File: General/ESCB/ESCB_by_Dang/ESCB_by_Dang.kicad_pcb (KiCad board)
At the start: 2 copper layers, 54.6 x 20.3 mm, 3 parts, among them J1 Power_Signal, J2 Motor

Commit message: Update
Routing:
- net GND: track 39.1 -> 41.2 mm
- net VCC: track 9.18 -> 10.7 mm
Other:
- board size 54.6 x 20.3 mm -> 52.6 x 20.3 mm
- net class Power: trace_width 0.5 -> 1
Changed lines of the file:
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@@
     (thickness 1.6)
     (drawings 7)
-    (tracks 22)
+    (tracks 24)
     (zones 0)
     (modules 3)
@@
   (net_class Power ""
     (clearance 0.2)
-    (trace_width 0.5)
+    (trace_width 1)
     (via_dia 0.8)
     (via_drill 0.4)
@@
     )
     (fp_text value Power_Signal (at 0 4.39 270) (layer F.Fab)
+      (effects (font (size 1 1) (thickness 0.15)))
+    )
+    (fp_circle (center -2 3.81) (end -1.9 3.81) (layer F.SilkS) (width 0.2))
+    (fp_circle (center -2 3.81) (end -1.9 3.81) (layer F.Fab) (width 0.2))
+    (fp_line (start -5.525 -3.1) (end 5.525 -3.1) (layer F.Fab) (width 0.1))
+    (fp_line (start 5.525 -3.1) (end 5.525 -2.4) (layer F.Fab) (width 0.1))
+    (fp_line (start 5.525 -2.4) (end 4.825 -2.4) (layer F.Fab) (width 0.1))
+    (fp_line (start 4.825 -2.4) (end 4.825 3.1) (layer F.Fab) (width 0.1))
+    (fp_line (start 4.825 3.1) (end -4.825 3.1) (layer F.Fab) (width 0.1))
+    (fp_line (start -4.825 3.1) (end -4.825 -2.4) (layer F.Fab) (width 0.1))
+    (fp_line (start -4.825 -2.4) (end -5.525 -2.4) (layer F.Fab) (width 0.1))
+    (fp_line (start -5.525 -2.4) (end -5.525 -3.1) (layer F.Fab) (width 0.1))
+    (fp_line (start -6.2 -3.35) (end 6.2 -3.35) (layer F.CrtYd) (width 0.05))
+    (fp_line (start 6.2 -3.35) (end 6.2 3.35) (layer F.CrtYd) (width 0.05))
+    (fp_line (start 6.2 3.35) (end -6.2 3.35) (layer F.CrtYd) (width 0.05))
+    (fp_line (start -6.2 3.35) (end -6.2 -3.35) (layer F.CrtYd) (width 0.05))
+    (fp_line (start -3.1 -3.1) (end 3.1 -3.1) (layer F.SilkS) (width 0.2))
+    (fp_line (start 4.825 3.1) (end -4.825 3.1) (layer F.SilkS) (width 0.2))
+    (fp_poly (pts (xy 3.5 -2.63) (xy 5.95 -2.63) (xy 5.95 -0.35) (xy 3.5 -0.35)) (layer F.Paste) (width 0.01))
+    (fp_poly (pts (xy 3.5 0.35) (xy 5.95 0.35) (xy 5.95 2.63) (xy 3.5 2.63)) (layer F.Paste) (width 0.01))
+    (fp_poly (pts (xy -5.95 -0.15) (xy -3.5 -0.15) (xy -3.5 2.13) (xy -5.95 2.13)) (layer F.Paste) (width 0.01))
+    (fp_poly (pts (xy -5.95 -3.13) (xy -3.5 -3.13) (xy -3.5 -0.85) (xy -5.95 -0.85)) (layer F.Paste) (width 0.01))
+    (pad 1 smd rect (at -2 0 270) (size 1.3 3.5) (layers F.Cu F.Paste F.Mask)
+      (net 1 GND))
+    (pad 2 smd rect (at 0 0 270) (size 1.3 3.5) (layers F.Cu F.Paste F.Mask)
+      (net 2 VCC))
+    (pad "" thru_hole circle (at -4 -1.5 270) (size 1.308 1.308) (drill 0.8) (layers *.Cu *.Mask))
+    (pad "" thru_hole circle (at -4 0.5 270) (size 1.308 1.308) (drill 0.8) (layers *.Cu *.Mask))
+    (pad "" thru_hole circle (at 4 -1 270) (size 1.308 1.308) (drill 0.8) (layers *.Cu *.Mask))
+    (pad "" thru_hole circle (at 4 1 270) (size 1.308 1.308) (drill 0.8) (layers *.Cu *.Mask))
+    (pad 3 smd rect (at 2 0 270) (size 1.3 3.5) (layers F.Cu F.Paste F.Mask)
+      (net 3 "Net-(J1-Pad3)"))
+    (model :extraparts3d:UMPS-03-03.5-T-VT-SM-WT.stp
+      (at (xyz 0 0 0))
+      (scale (xyz 1 1 1))
+      (rotate (xyz -90 0 0))
+    )
+  )
+  (module extraparts:Samtec_mPOWER_UMPS_3pin (layer F.Cu)
+    (at 164.9 93.98 90)
+    (fp_text reference J2 (at 7.62 -2.34) (layer F.SilkS)
+      (effects (font (size 1 1) (thickness 0.15)))
+    )
+    (fp_text value Motor (at 0 5.28 90) (layer F.Fab)
       (effects (font (size 1 1) (thickness 0.15)))
     )
@@
     (fp_circle (center -2 3.81) (end -1.9 3.81) (layer F.Fab) (width 0.2))
     (fp_circle (center -2 3.81) (end -1.9 3.81) (layer F.SilkS) (width 0.2))
-    (pad 1 smd rect (at -2 0 270) (size 1.3 3.5) (layers F.Cu F.Paste F.Mask)
-      (net 1 GND))
-    (pad 2 smd rect (at 0 0 270) (size 1.3 3.5) (layers F.Cu F.Paste F.Mask)
-      (net 2 VCC))
-    (pad "" thru_hole circle (at -4 -1.5 270) (size 1.308 1.308) (drill 0.8) (layers *.Cu *.Mask))
-    (pad "" thru_hole circle (at -4 0.5 270) (size 1.308 1.308) (drill 0.8) (layers *.Cu *.Mask))
-    (pad "" thru_hole circle (at 4 -1 270) (size 1.308 1.308) (drill 0.8) (layers *.Cu *.Mask))
-    (pad "" thru_hole circle (at 4 1 270) (size 1.308 1.308) (drill 0.8) (layers *.Cu *.Mask))
-    (pad 3 smd rect (at 2 0 270) (size 1.3 3.5) (layers F.Cu F.Paste F.Mask)
-      (net 3 "Net-(J1-Pad3)"))
-    (model :extraparts3d:UMPS-03-03.5-T-VT-SM-WT.stp
-      (at (xyz 0 0 0))
-      (scale (xyz 1 1 1))
-      (rotate (xyz -90 0 0))
-    )
-  )
-  (module extraparts:Samtec_mPOWER_UMPS_3pin (layer F.Cu)
-    (at 164.9 93.98 90)
-    (fp_text reference J2 (at -3.81 5.28 270) (layer F.SilkS)
-      (effects (font (size 1 1) (thickness 0.15)))
-    )
-    (fp_text value Motor (at 0 5.28 90) (layer F.Fab)
-      (effects (font (size 1 1) (thickness 0.15)))
-    )
-    (fp_circle (center -2 3.81) (end -1.9 3.81) (layer F.SilkS) (width 0.2))
-    (fp_circle (center -2 3.81) (end -1.9 3.81) (layer F.Fab) (width 0.2))
-    (fp_line (start -5.525 -3.1) (end 5.525 -3.1) (layer F.Fab) (width 0.1))
-    (fp_line (start 5.525 -3.1) (end 5.525 -2.4) (layer F.Fab) (width 0.1))
-    (fp_line (start 5.525 -2.4) (end 4.825 -2.4) (layer F.Fab) (width 0.1))
-    (fp_line (start 4.825 -2.4) (end 4.825 3.1) (layer F.Fab) (width 0.1))
-    (fp_line (start 4.825 3.1) (end -4.825 3.1) (layer F.Fab) (width 0.1))
-    (fp_line (start -4.825 3.1) (end -4.825 -2.4) (layer F.Fab) (width 0.1))
-    (fp_line (start -4.825 -2.4) (end -5.525 -2.4) (layer F.Fab) (width 0.1))
-    (fp_line (start -5.525 -2.4) (end -5.525 -3.1) (layer F.Fab) (width 0.1))
-    (fp_line (start -6.2 -3.35) (end 6.2 -3.35) (layer F.CrtYd) (width 0.05))
-    (fp_line (start 6.2 -3.35) (end 6.2 3.35) (layer F.CrtYd) (width 0.05))
-    (fp_line (start 6.2 3.35) (end -6.2 3.35) (layer F.CrtYd) (width 0.05))
-    (fp_line (start -6.2 3.35) (end -6.2 -3.35) (layer F.CrtYd) (width 0.05))
-    (fp_line (start -3.1 -3.1) (end 3.1 -3.1) (layer F.SilkS) (width 0.2))
-    (fp_line (start 4.825 3.1) (end -4.825 3.1) (layer F.SilkS) (width 0.2))
-    (fp_poly (pts (xy 3.5 -2.63) (xy 5.95 -2.63) (xy 5.95 -0.35) (xy 3.5 -0.35)) (layer F.Paste) (width 0.01))
-    (fp_poly (pts (xy 3.5 0.35) (xy 5.95 0.35) (xy 5.95 2.63) (xy 3.5 2.63)) (layer F.Paste) (width 0.01))
-    (fp_poly (pts (xy -5.95 -0.15) (xy -3.5 -0.15) (xy -3.5 2.13) (xy -5.95 2.13)) (layer F.Paste) (width 0.01))
-    (fp_poly (pts (xy -5.95 -3.13) (xy -3.5 -3.13) (xy -3.5 -0.85) (xy -5.95 -0.85)) (layer F.Paste) (width 0.01))
     (pad 3 smd rect (at 2 0 90) (size 1.3 3.5) (layers F.Cu F.Paste F.Mask)
       (net 4 "Net-(J2-Pad3)"))
@@
       (effects (font (size 1 1) (thickness 0.15)))
     )
+    (fp_line (start 16 -8.6) (end -16 -8.6) (layer F.SilkS) (width 0.12))
+    (fp_line (start -16 -8.6) (end -16 8.6) (layer F.SilkS) (width 0.12))
+    (fp_line (start -16 8.6) (end 16 8.6) (layer F.SilkS) (width 0.12))
     (fp_line (start 16 8.6) (end 16 -8.6) (layer F.SilkS) (width 0.12))
-    (fp_line (start -16 8.6) (end 16 8.6) (layer F.SilkS) (width 0.12))
-    (fp_line (start -16 -8.6) (end -16 8.6) (layer F.SilkS) (width 0.12))
-    (fp_line (start 16 -8.6) (end -16 -8.6) (layer F.SilkS) (width 0.12))
     (pad 1 smd rect (at 14.5 6.55 180) (size 3 4) (layers F.Cu F.Paste F.Mask)
       (net 1 GND))
@@
       (net 5 "Net-(J2-Pad2)"))
   )
-  (gr_text "Motor\n" (at 170.18 93.98 90) (layer F.SilkS)
+  (gr_text "Motor\n" (at 166.37 86.36) (layer F.SilkS)
     (effects (font (size 1 1) (thickness 0.15)))
   )
@@
     (effects (font (size 1 1) (thickness 0.15)))
   )
-  (gr_line (start 171.45 82.55) (end 116.84 82.55) (layer Edge.Cuts) (width 0.05))
-  (gr_line (start 171.45 102.87) (end 171.45 82.55) (layer Edge.Cuts) (width 0.05))
-  (gr_line (start 116.84 102.87) (end 171.45 102.87) (layer Edge.Cuts) (width 0.05))
+  (gr_line (start 169.45 82.55) (end 116.84 82.55) (layer Edge.Cuts) (width 0.05))
+  (gr_line (start 169.45 102.87) (end 169.45 82.55) (layer Edge.Cuts) (width 0.05))
+  (gr_line (start 116.84 102.87) (end 169.45 102.87) (layer Edge.Cuts) (width 0.05))
   (gr_line (start 116.84 82.55) (end 116.84 102.87) (layer Edge.Cuts) (width 0.05))
   (segment (start 127.69 89.04) (end 127.69 87.200001) (width 0.5) (layer F.Cu) (net 1))
-  (segment (start 124.75 91.98) (end 127.69 89.04) (width 0.5) (layer F.Cu) (net 1))
-  (segment (start 122.5 91.98) (end 124.75 91.98) (width 0.5) (layer F.Cu) (net 1))
   (segment (start 153.99 87.200001) (end 157.19 84.000001) (width 0.5) (layer F.Cu) (net 1))
   (segment (start 127.69 87.200001) (end 153.99 87.200001) (width 0.5) (layer F.Cu) (net 1))
-  (segment (start 127.69 97.959998) (end 127.69 100.300001) (width 0.5) (layer F.Cu) (net 2))
-  (segment (start 123.710002 93.98) (end 127.69 97.959998) (width 0.5) (layer F.Cu) (net 2))
+  (segment (start 127.69 89.54) (end 127.69 87.200001) (width 1) (layer F.Cu) (net 1))
+  (segment (start 125.25 91.98) (end 127.69 89.54) (width 1) (layer F.Cu) (net 1))
+  (segment (start 122.5 91.98) (end 125.25 91.98) (width 1) (layer F.Cu) (net 1))
   (segment (start 122.5 93.98) (end 123.710002 93.98) (width 0.5) (layer F.Cu) (net 2))
+  (segment (start 127.69 97.509998) (end 127.69 100.300001) (width 1) (layer F.Cu) (net 2))
+  (segment (start 124.160002 93.98) (end 127.69 97.509998) (width 1) (layer F.Cu) (net 2))
+  (segment (start 122.5 93.98) (end 124.160002 93.98) (width 1) (layer F.Cu) (net 2))
   (segment (start 120.11 95.98) (end 119.38 95.25) (width 0.25) (layer F.Cu) (net 3))
   (via (at 119.38 95.25) (size 0.8) (drill 0.4) (layers F.Cu B.Cu) (net 3))

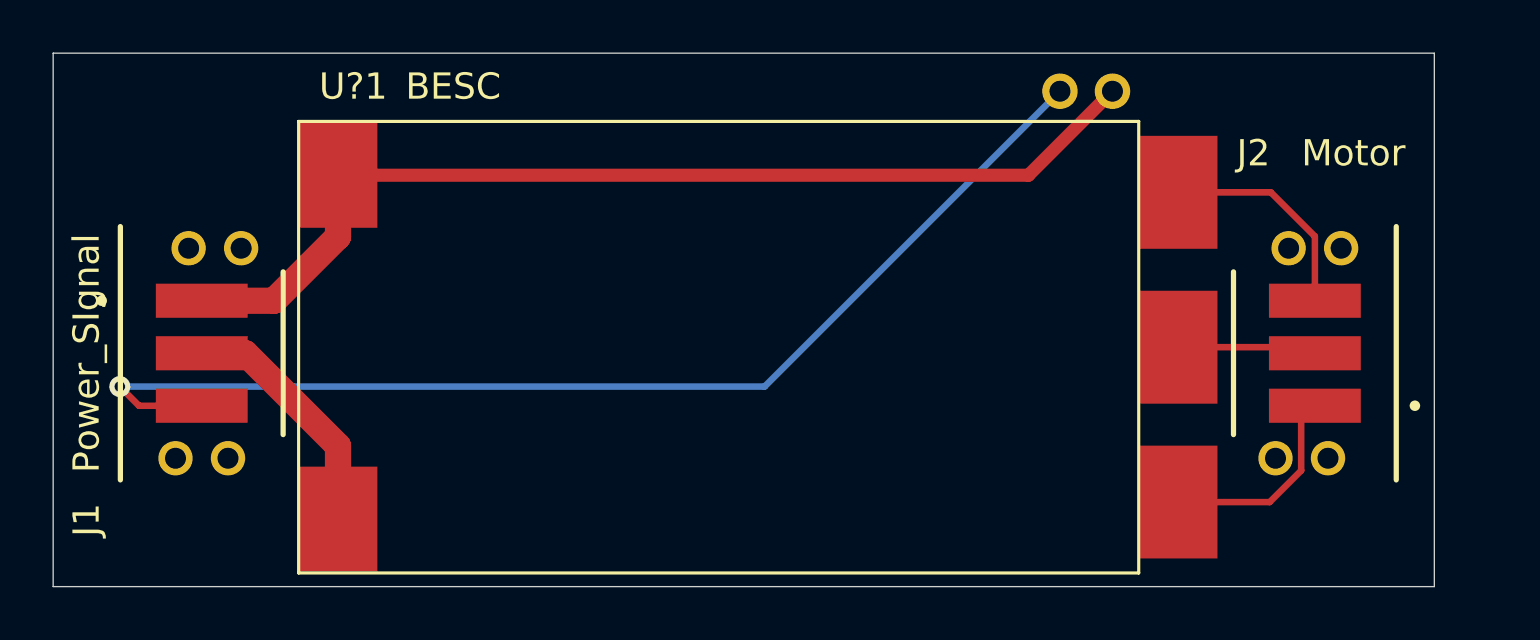
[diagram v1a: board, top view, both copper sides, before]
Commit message: Fixed Power Route Width
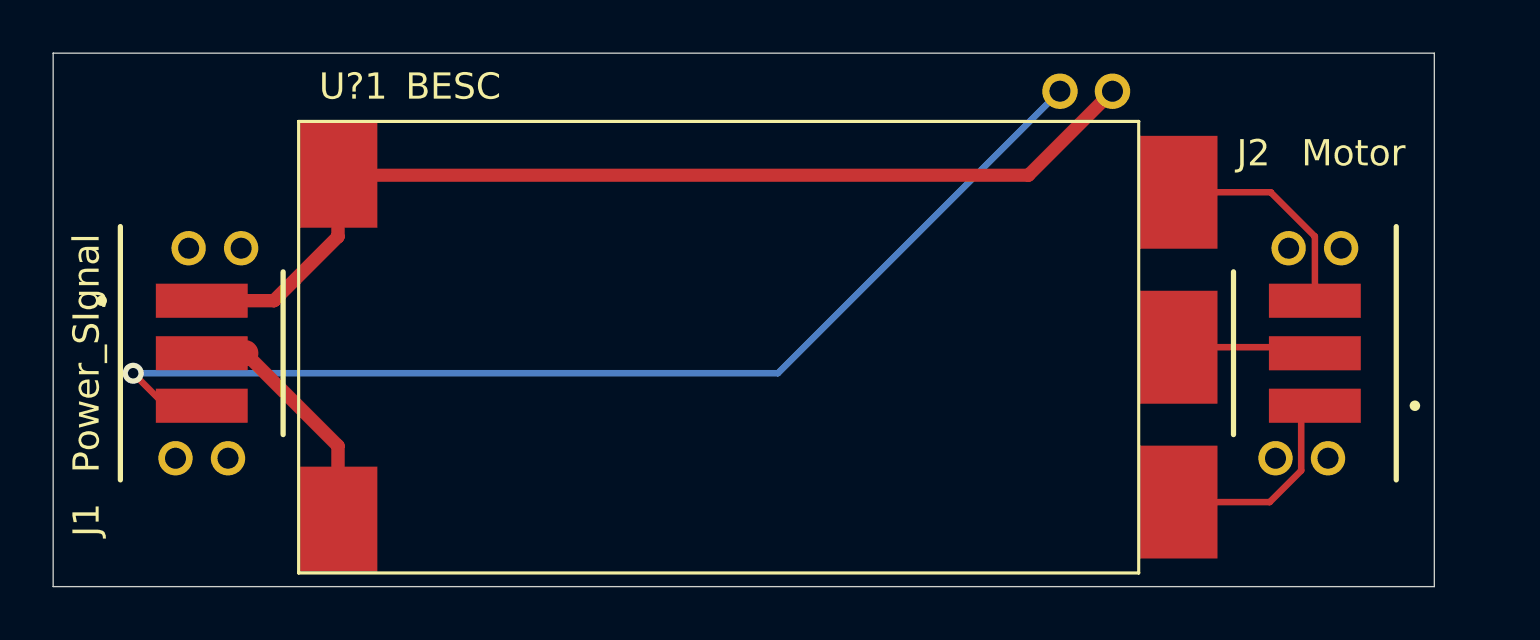
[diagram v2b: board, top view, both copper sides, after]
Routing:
- net Net-(J1-Pad3): track 43.9 -> 42.9 mm
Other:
- net class Power: trace_width 1 -> 0.508
